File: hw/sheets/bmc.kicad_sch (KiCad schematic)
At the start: 20 parts, among them SW1 SSSS711403, SW2 SSSS711403, U10 TS5A3166, U11 DIP-8 Socket, U12 TPS2053BDR, U13 W25Q32JVSS, U15 TCA9555PWR, U8 ESP32-S3-WROOM-1-N16R2, U9 TS5A3166

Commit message: Fix D1/D2 and U13 footprint references (didn't exist in any library)
Found while auditing every footprint reference in CONNECTIONS.txt against
the actual installed libraries (fp-lib-table + on-disk .kicad_mod files),
prompted by the earlier PCB pass's substituted-footprint workaround note:

- D1/D2 (PMEG2010ER): hardcoded Diode_SMD:D_SOD-123W, which doesn't exist
  anywhere, and Diode_SMD wasn't even registered in fp-lib-table. Fixed to
  Diode_SMD:Nexperia_CFP3_SOD-123W (the real footprint for this Nexperia
  part's actual package) and registered the library.
- U13 (W25Q32JVSS): hardcoded Package_SO:SOIC-8_5.23x5.23mm_P1.27mm --
  close but not the real footprint name, Package_SO:SOIC-8_5.3x5.3mm_P1.27mm.

Verified: netlist diff shows only these 3 footprint string changes,
nothing else moved (component count, all pin-net assignments unchanged).
ERC footprint_link_issues: 3 -> 0, no other category changed. PCB rebuild:
still just the 1 expected J6 case, DRC unchanged at 20 pre-existing
fine-pitch clearance violations. Schematic quadrant layout still at 0mm
drift.
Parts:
- U13: footprint Package_SO:SOIC-8_5.23x5.23mm_P1.27mm -> Package_SO:SOIC-8_5.3x5.3mm_P1.27mm
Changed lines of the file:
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@@
 		(property "Reference" "U13" (at 165.10000000000002 154.94 0) (effects (font (size 1.27 1.27))))
 		(property "Value" "W25Q32JVSS" (at 165.10000000000002 157.48 0) (effects (font (size 1.27 1.27))))
-		(property "Footprint" "Package_SO:SOIC-8_5.23x5.23mm_P1.27mm" (at 177.8 167.64 0) (effects (font (size 1.27 1.27)) hide))
+		(property "Footprint" "Package_SO:SOIC-8_5.3x5.3mm_P1.27mm" (at 177.8 167.64 0) (effects (font (size 1.27 1.27)) hide))
 	)
 	(symbol (lib_id "power:GND") (at 177.8 177.8 0) (unit 1)

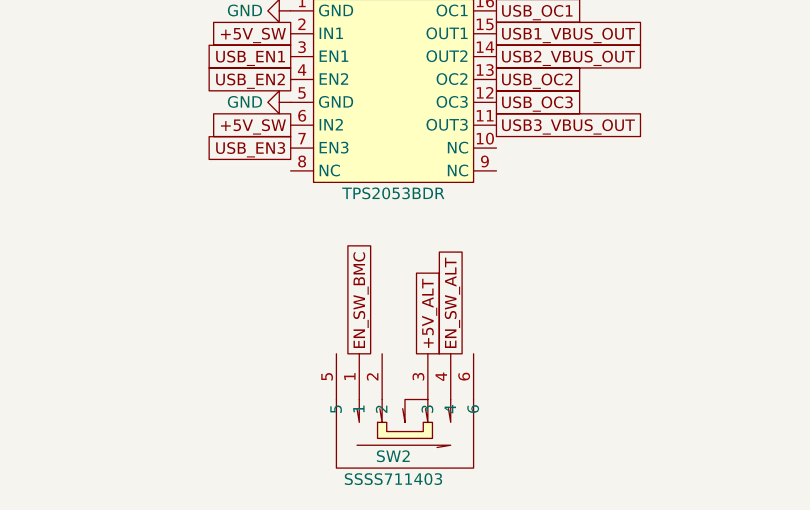
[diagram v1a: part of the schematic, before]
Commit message: Carrier board: audio/FPC pinout fixes matching 3.3, SW2 remap, UART1 breakout, real PCB layout
Schematic fixes (verified pin-for-pin against TeaCup(C)3.3's real netlist,
not assumed):
- J6 audio jack: R1/R2 -> HPOUTL/GND, S -> MICLP, matching 3.3's J10 exactly
  (previous wiring incorrectly tied GND to a schematic pin, G, with no
  matching pad on the real Jack_3.5mm_PJ320D_Horizontal footprint).
- J7/J8 FPC camera connectors: full pin-for-pin remap to match 3.3's real
  J13 pinout -- the previous "standard RPi/Arducam" pinout had power/ground
  swapped, clock/data lanes in the wrong order, and reversed differential
  polarity throughout. Added JP11/JP12 sensor-enable select jumpers
  (GPIO vs hardwired +3V3), replicating 3.3's J15.
- J1 MIPI0/MIPI1 pin order on the connector reordered (CLK/D1/D0, P-before-N)
  to match J7/J8's now-fixed order, so routing between them doesn't need to
  cross over itself.
- HPOUTL relocated from J1 pin 58 (isolated, far from any other audio net)
  down to sit beside MICLP at pins 170-172, geography-first per
  UNIVERSAL.md SS8.
- SW2 (manual power-override switch) throw1/throw4 swapped: throw1 now
  forces ALT, throw4 now forces BMC.
- New J36 header breaks out UART1 (the BMC-ESP32<->J1 console link) for
  external monitoring, same as UART0/2/3 already had.

All verified via isolated before/after ERC diffs -- each change nets to
either 0 or a fully-explained delta against the 429-violation baseline,
never an unexplained regression.

PCB: teacup-carrier.kicad_pcb replaced with the manually-laid-out board
(previously developed as a separate merge-test attempt): real component
placement grouped by circuit block, board outline resized twice to
snugly enclose the layout, GND copper pour on both F.Cu and B.Cu, and
mounting holes repositioned to match. The old rough auto-placed board is
gone.
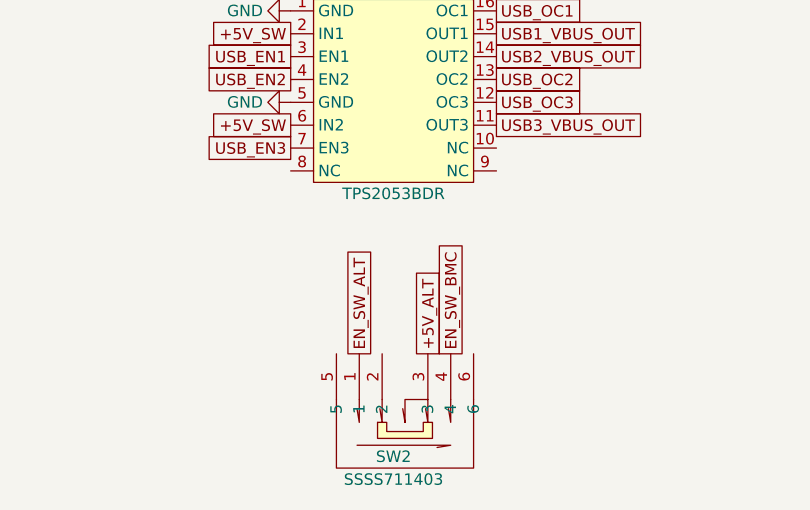
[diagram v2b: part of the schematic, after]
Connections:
- net EN_SW_ALT: now also SW2.1; no longer SW2.4
- net EN_SW_BMC: now also SW2.4; no longer SW2.1
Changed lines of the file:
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@@
 	(global_label "SW_SENSE_1" (at 203.2 135.89 270) (effects (font (size 1.27 1.27)) (justify right)))
 	(global_label "SW_SENSE_4" (at 214.63 135.89 270) (effects (font (size 1.27 1.27)) (justify right)))
-	(global_label "EN_SW_BMC" (at 173.99 273.05 90) (effects (font (size 1.27 1.27)) (justify left)))
+	(global_label "EN_SW_ALT" (at 173.99 273.05 90) (effects (font (size 1.27 1.27)) (justify left)))
 	(global_label "+5V_ALT" (at 181.61 273.05 90) (effects (font (size 1.27 1.27)) (justify left)))
-	(global_label "EN_SW_ALT" (at 184.15 273.05 90) (effects (font (size 1.27 1.27)) (justify left)))
+	(global_label "EN_SW_BMC" (at 184.15 273.05 90) (effects (font (size 1.27 1.27)) (justify left)))
 	(global_label "NOR_U4_CE" (at 165.1 165.1 180) (effects (font (size 1.27 1.27)) (justify right)))
 	(global_label "SFC_IO1" (at 190.5 165.1 0) (effects (font (size 1.27 1.27)) (justify left)))
